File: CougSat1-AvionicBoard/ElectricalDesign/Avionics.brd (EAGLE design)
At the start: 160 x 100 mm, 213 parts, among them J1 +X Panel GPS, J10 iFJR SD1, J11 -Y, J12 +Z, J13 +X, J14 -Z, J15 +Y, J16 IFJR SD0, J2 IHU SD1, J3 SWD, J4 CougSat Card, J5 -X, J6 IHU SD0, J8 SWD, J9 SWD, U1 STM32L476RGT, U10 BNO055, U11 M24M01, U12 TXS0102DQM, U13 TXS0102DQM, U14 AD8515, U15 BNO055, U16 BNO055, U17 TXS0102DQM, U18 TXS0102DQM, U19 AD8515, U2 STM32L476RGT, U20 INA199C2, U21 INA199C2, U22 TXS0102DQM, U23 TXS0102DQM, U24 AD8515, U25 AD7291, U26 AD7291, U27 TXS0102DQM, U28 INA199C2, U29 AD8515, U3 STM32L476RGT, U30 DRV8837, U4 M24M01, U5 TXS0102DQM, U6 DRV8837, U7 DRV8837, U8 AD7291, U9 Venus838FLPx-L, Y1 8MHz ±10ppm, Y10 32.768kHz ±10ppm, Y2 32.768kHz ±10ppm, Y3 8MHz ±10ppm, Y4 32.768kHz ±10ppm, Y5 8MHz ±10ppm, Y6 32.768kHz ±10ppm, Y7 32.768kHz ±10ppm, Y8 32.768kHz ±10ppm

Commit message: Removed CTRL_RESET
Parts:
- moved R13 207.9 mm to (95.2, 218.5), turned to 90 degrees
- moved R4 205.7 mm to (112.9, 224.9)
- moved L1 191.6 mm to (112.9, 218.3)
- moved DS1 157.7 mm to (94.3, 221.2), turned to 180 degrees
- moved J4 117.0 mm to (0.00, 0.00)
- moved U2 9.32 mm to (66.8, 205.9)
- moved R43 3.50 mm to (79.0, 182.1)
- moved C4 0.20 mm to (90.7, 186.8)
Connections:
- removed net CTRL_!RESET: J4.A41, J4.B41, U1.37, U2.10, U3.38
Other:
- board size 160 x 100 mm -> 90.4 x 95.8 mm

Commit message: Placed Large Components
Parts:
- J4: device CougsInSpace-Boards:CARD-FULL-OPEN+X -> CougsInSpace-Boards:CARD-FULL
- moved J14 343.4 mm to (70.5, -38.0), turned to 90 degrees
- moved C16 329.8 mm to (64.9, -6.80), flipped to the bottom, turned to 270 degrees
- moved C12 324.4 mm to (86.1, 5.90), flipped to the bottom, turned to 270 degrees
- moved C60 322.9 mm to (56.0, -13.6), flipped to the bottom, turned to 180 degrees
- moved C61 321.3 mm to (49.5, -13.6), flipped to the bottom, turned to 180 degrees
- moved C63 318.4 mm to (56.5, 1.60), flipped to the bottom
- moved C62 312.2 mm to (45.4, -2.50), flipped to the bottom, turned to 270 degrees
- moved R36 311.6 mm to (45.5, 25.3), flipped to the bottom, turned to 270 degrees
- moved C9 310.5 mm to (64.9, -3.80), flipped to the bottom, turned to 270 degrees
- moved C21 310.2 mm to (52.4, 26.5), flipped to the bottom, turned to 180 degrees
- moved C11 310.0 mm to (76.9, 13.5), flipped to the bottom, turned to 180 degrees
- moved C20 305.4 mm to (49.5, 26.5), flipped to the bottom
- moved C10 304.3 mm to (72.9, 14.1), flipped to the bottom, turned to 90 degrees
- moved C83 303.5 mm to (46.1, -37.8), flipped to the bottom, turned to 90 degrees
- moved J11 303.2 mm to (47.5, -38.0), turned to 90 degrees
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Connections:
- new net IHU_GPIO-6: J4.A41, U3.37
- new net IHU_GPIO-7: J4.B41, U3.38
- net ADCS_BUS_SCL: now also U5.3; no longer U5.2
- net ADCS_BUS_SDA: now also U5.2; no longer U5.3
- net ADCS_JTCK: now also U12.3; no longer U12.2
- net ADCS_JTDI: now also U12.2; no longer U12.3
- net BUS_I2C0_SCL: now also U5.6; no longer U5.7
- net BUS_I2C0_SDA: now also U5.7; no longer U5.6
- net IFJR_BUS_MISO: now also U23.2; no longer U23.3
- net IFJR_BUS_SCK: now also U23.3; no longer U23.2
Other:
- outline, holes or cut-outs redrawn

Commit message: Finished Placing Components, Began Wiring
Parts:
- added C100, C101, C102, C43, C84, C99: 100nF 10%, CougsInSpace-Capacitors:1608
- moved C70 367.8 mm to (85.7, -14.1), flipped to the bottom, turned to 180 degrees
- moved C69 366.4 mm to (85.7, -15.8), flipped to the bottom, turned to 180 degrees
- moved C65 356.1 mm to (81.6, -19.9), flipped to the bottom, turned to 270 degrees
- moved C64 351.4 mm to (81.6, -17.0), flipped to the bottom, turned to 90 degrees
- moved C15 343.4 mm to (74.4, -19.9), flipped to the bottom, turned to 270 degrees
- moved R38 339.1 mm to (34.2, -14.7), flipped to the bottom, turned to 180 degrees
- moved C23 336.7 mm to (33.5, -19.8), flipped to the bottom, turned to 270 degrees
- moved R37 334.7 mm to (45.6, -2.60), flipped to the bottom, turned to 90 degrees
- moved C18 333.5 mm to (65.7, -4.20), flipped to the bottom, turned to 180 degrees
- moved R31 333.3 mm to (86.0, 19.9), flipped to the bottom
- moved C17 329.1 mm to (65.7, -1.80), flipped to the bottom, turned to 180 degrees
- moved C19 329.0 mm to (59.0, -0.80), flipped to the bottom, turned to 90 degrees
- moved U29 327.7 mm to (86.2, -19.0), flipped to the bottom, turned to 270 degrees
- moved U7 327.7 mm to (86.5, 15.5), flipped to the bottom, turned to 270 degrees
- moved R30 326.6 mm to (80.4, 19.9), flipped to the bottom
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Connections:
- removed net AVDD: C85.1, C86.1, C87.1
- net 3.3V_0: now also C101.1, C99.1
- net 3.3V_5: now also C100.1, C102.1
- net AGND: now also C43.2, C84.2
- net AVDD-0: now also C43.1, C85.1, C86.1, C87.1
- net AVDD-1: now also C84.1
- net DGND: now also C100.2, C101.2, C102.2, C99.2
- net IFJR_BUS_CS: now also U27.2; no longer U27.3
- net IFJR_BUS_MOSI: now also U27.3; no longer U27.2
- net IHU_JTCK: now also U17.3; no longer U17.2
- net IHU_JTDI: now also U17.2; no longer U17.3
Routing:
- net DGND: track 0.00 -> 61.0 mm
- net 3.3V_0: track 0.00 -> 11.6 mm
- net 3.3V_5: track 0.00 -> 8.23 mm
- net IHU_OSC_OUT: track 0.00 -> 4.56 mm
- net IFJR_OSC_OUT: track 0.00 -> 4.56 mm
- net 3.3V_2: track 0.00 -> 4.11 mm
- net IHU_SD_CS1: track 0.00 -> 3.55 mm
- net IFJR_OSC_32_IN: track 0.00 -> 2.07 mm
- net IFJR_OSC_32_OUT: track 0.00 -> 2.07 mm
- net IHU_OSC_32_IN: track 0.00 -> 2.07 mm
- net IHU_OSC_32_OUT: track 0.00 -> 2.07 mm
- net IHU_OSC_IN: track 0.00 -> 2.07 mm
- net IFJR_OSC_IN: track 0.00 -> 2.07 mm
- net IHU_SD_CS0: track 0.00 -> 2.02 mm
- net IHU_BOOT0: track 0.00 -> 1.93 mm
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
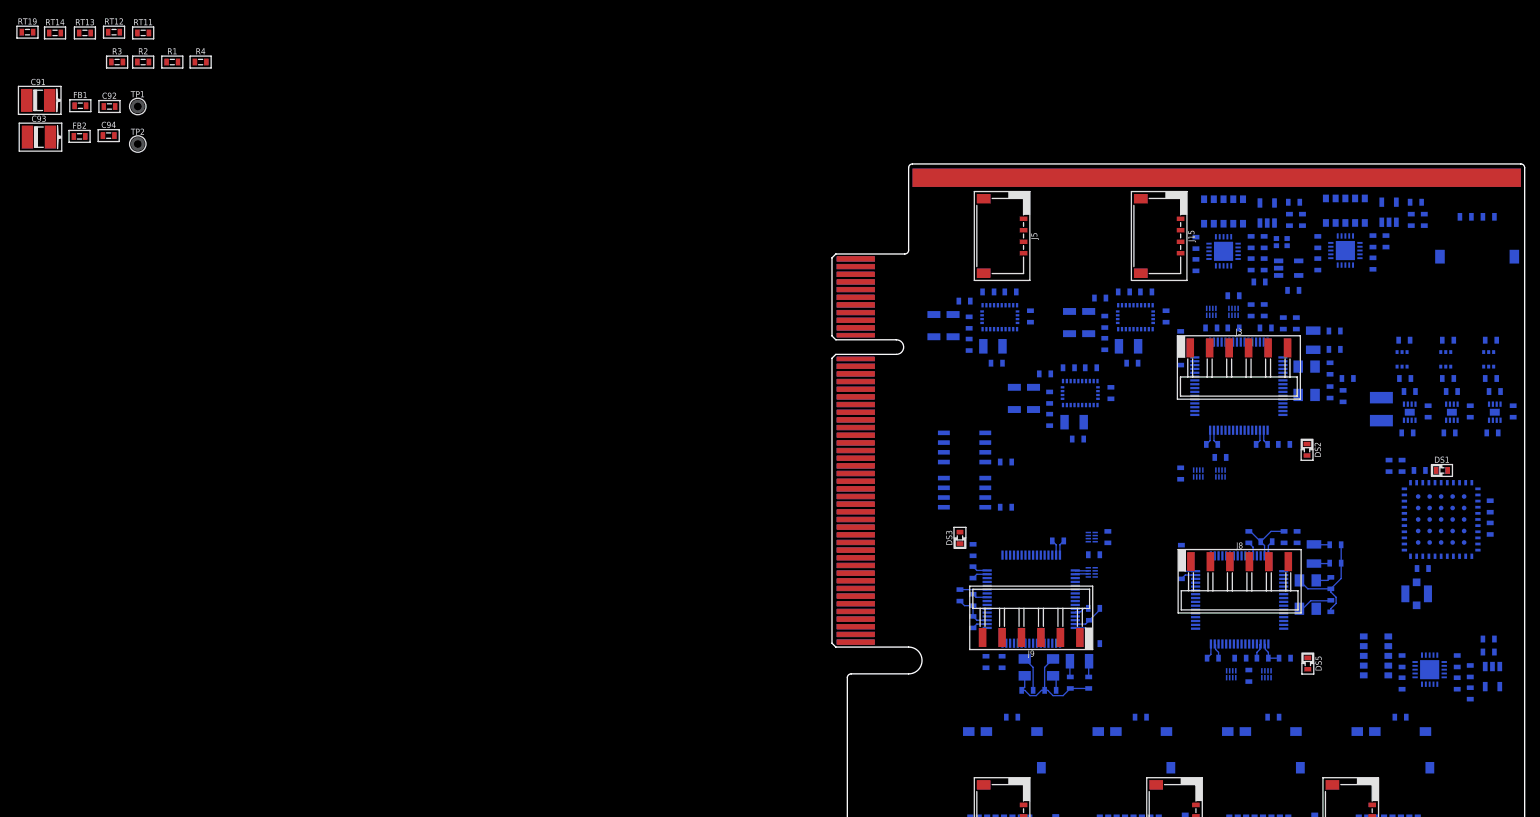
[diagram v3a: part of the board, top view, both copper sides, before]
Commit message: Placed AVDD Circuits and Ground Straps
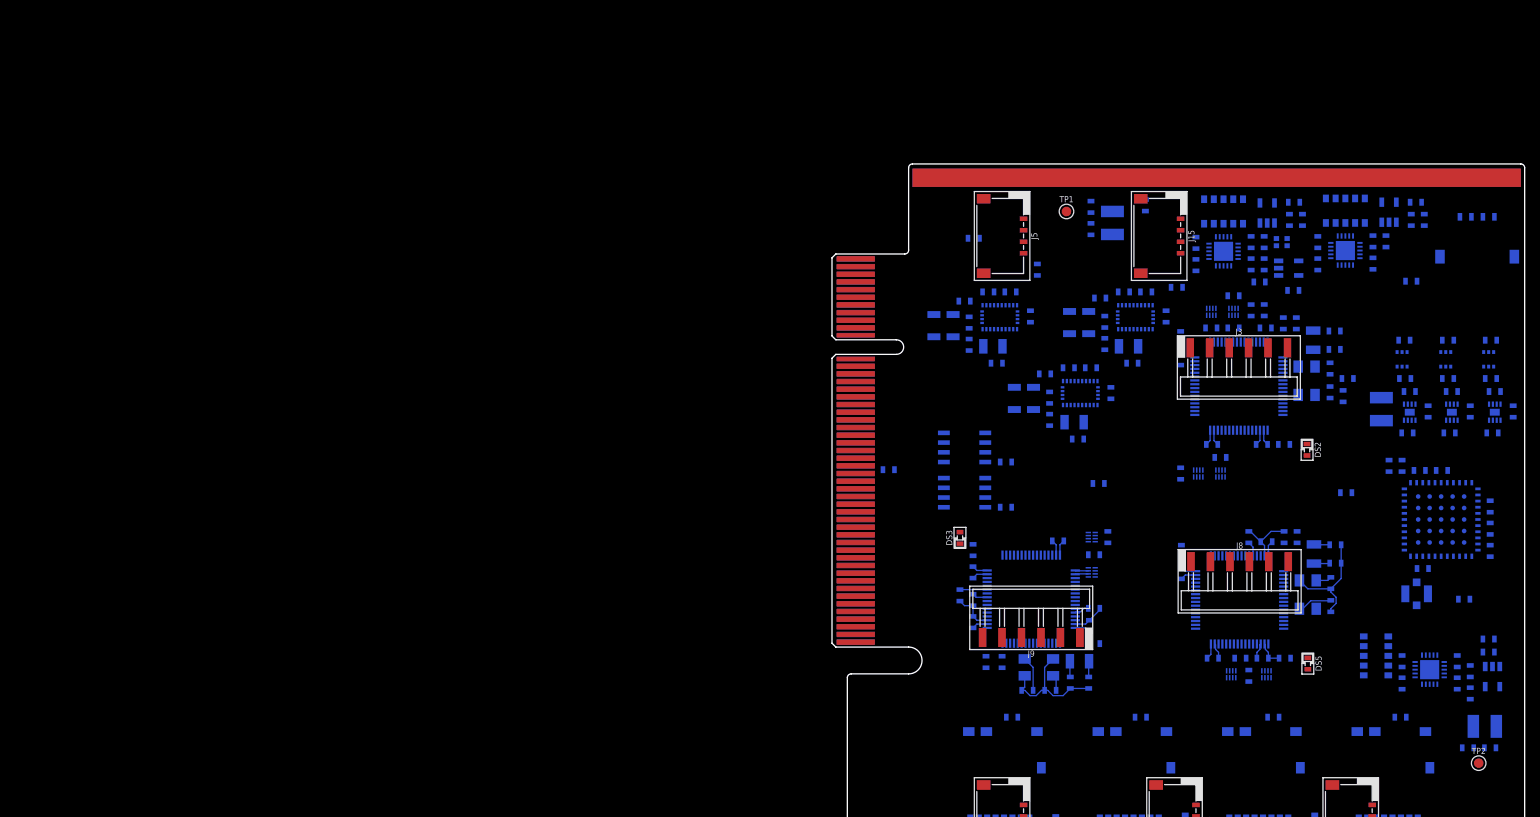
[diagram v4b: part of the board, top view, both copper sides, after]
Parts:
- TP1, TP2: value TEST_POINT-THT-1.0 -> TEST_POINT-SMD-C-1.25; device CougsInSpace-Connectors:THT-1.0 -> CougsInSpace-Connectors:SMD-C-1.25
- moved C93 203.8 mm to (85.2, -25.5), flipped to the bottom
- moved FB2 198.0 mm to (83.0, -28.3), flipped to the bottom, turned to 180 degrees
- moved C94 197.2 mm to (85.9, -28.3), flipped to the bottom, turned to 180 degrees
- moved RT13 194.6 mm to (82.5, -8.90), flipped to the bottom
- moved TP2 192.8 mm to (84.4, -30.3)
- moved RT19 182.3 mm to (67.1, 5.00), flipped to the bottom
- moved R4 180.0 mm to (85.9, -2.60), flipped to the bottom, turned to 90 degrees
- moved RT11 168.6 mm to (75.6, 32.6), flipped to the bottom
- moved RT14 148.4 mm to (34.8, 6.20), flipped to the bottom
- moved C91 141.1 mm to (36.6, 40.2), flipped to the bottom, turned to 90 degrees
- moved R2 138.1 mm to (45.0, 31.8), flipped to the bottom
- moved FB1 132.6 mm to (33.8, 42.3), flipped to the bottom, turned to 270 degrees
- moved C92 129.1 mm to (33.8, 39.4), flipped to the bottom, turned to 270 degrees
- moved R3 123.1 mm to (26.8, 34.1), flipped to the bottom, turned to 270 degrees
- moved TP1 122.0 mm to (30.6, 41.7)
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
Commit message: Routed Most Traces
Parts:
- removed C44, C51, C67: 1µF 10%, CougsInSpace-Capacitors:1608
- removed C50, C52, C68: 100nF 10%, CougsInSpace-Capacitors:1608
- moved C70 82.3 mm to (4.40, -26.9), turned to 90 degrees
- moved C69 80.4 mm to (6.10, -26.9), turned to 90 degrees
- moved U29 77.3 mm to (9.30, -26.4), turned to 180 degrees
- moved C64 75.6 mm to (7.30, -31.0), turned to 0 degrees
- moved C88 75.5 mm to (8.60, -29.3), turned to 180 degrees
- moved TP2 74.8 mm to (10.3, -20.2)
- moved C94 73.5 mm to (13.0, -19.3), turned to 0 degrees
- moved C65 72.3 mm to (10.2, -31.0), turned to 180 degrees
- moved C84 72.3 mm to (11.5, -29.3), turned to 180 degrees
- moved C93 71.6 mm to (13.7, -22.1), turned to 180 degrees
- moved U26 71.5 mm to (8.40, -34.6), turned to 180 degrees
- moved R7 70.4 mm to (7.30, -38.2), turned to 0 degrees
- moved RN3 69.2 mm to (6.60, -41.6), turned to 0 degrees
- moved FB2 67.7 mm to (15.9, -19.3), turned to 0 degrees
- moved C15 66.8 mm to (10.2, -38.2), turned to 180 degrees
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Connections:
- removed net COIL-X_OUT1: R29.1, U20.4, U30.2
- removed net COIL-Y_OUT1: R30.1, U21.4, U6.2
- removed net COIL-Z_OUT1: R31.1, U28.4, U7.2
- new net COIL-X_OUT2: R29.1, U20.4, U30.3
- new net COIL-Y_OUT2: R30.1, U21.4, U6.3
- new net COIL-Z_OUT2: R31.1, U28.4, U7.3
- net ADCS_ADC0_VREF: no longer RN1.3
- net ADCS_HALF_REF: no longer C44.1, C50.1
- net AGND: no longer C44.2, C50.2, C51.2, C52.2, C67.2, C68.2
- net AVREF-0: now also RN1.3; no longer C51.1, C52.1
- net AVREF-1: no longer C67.1, C68.1
- net COIL-X_!SLEEP: now also U2.27; no longer U2.20
- net COIL-X_COIL+: now also U30.2; no longer R29.2, U20.5
- net COIL-X_COIL-: now also R29.2, U20.5; no longer U30.3
- net COIL-X_IN1: now also U2.16; no longer U2.14
- net COIL-X_IN2: now also U2.17; no longer U2.15
- net COIL-Y_!SLEEP: now also U2.20; no longer U2.27
- net COIL-Y_COIL+: now also U6.2; no longer R30.2, U21.5
- net COIL-Y_COIL-: now also R30.2, U21.5; no longer U6.3
- net COIL-Y_IN1: now also U2.14; no longer U2.16
- net COIL-Y_IN2: now also U2.15; no longer U2.17
- net COIL-Z_COIL+: now also U7.2; no longer R31.2, U28.5
- net COIL-Z_COIL-: now also R31.2, U28.5; no longer U7.3
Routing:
- net DGND: track 61.0 -> 713.3 mm, vias 0 -> 85
- net 3.3V_2: track 4.11 -> 381.3 mm, vias 0 -> 43
- net AGND: track 0.00 -> 338.0 mm, vias 0 -> 33
- net ADCS_I2C1_SCL: track 0.00 -> 319.8 mm, vias 0 -> 2
- net ADCS_I2C1_SDA: track 0.00 -> 318.1 mm, vias 0 -> 3
- net PGND: track 0.00 -> 238.6 mm, vias 0 -> 9
- net COIL-Y_COIL+: track 0.00 -> 212.6 mm, vias 0 -> 3
- net COIL-Y_COIL-: track 0.00 -> 210.8 mm, vias 0 -> 3
- net CHASSIS: track 0.00 -> 204.6 mm, vias 0 -> 2
- net 3.3V_0: track 11.6 -> 189.5 mm, vias 0 -> 29
- net COIL-Z_COIL+: track 0.00 -> 177.2 mm, vias 0 -> 3
- net COIL-Z_COIL-: track 0.00 -> 173.1 mm, vias 0 -> 3
- net VBATT_5: track 0.00 -> 167.2 mm, vias 0 -> 4
- net 3.3V_5: track 8.23 -> 155.5 mm, vias 0 -> 20
- net BUS_JTAG_TMS: track 0.00 -> 132.1 mm, vias 0 -> 6
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
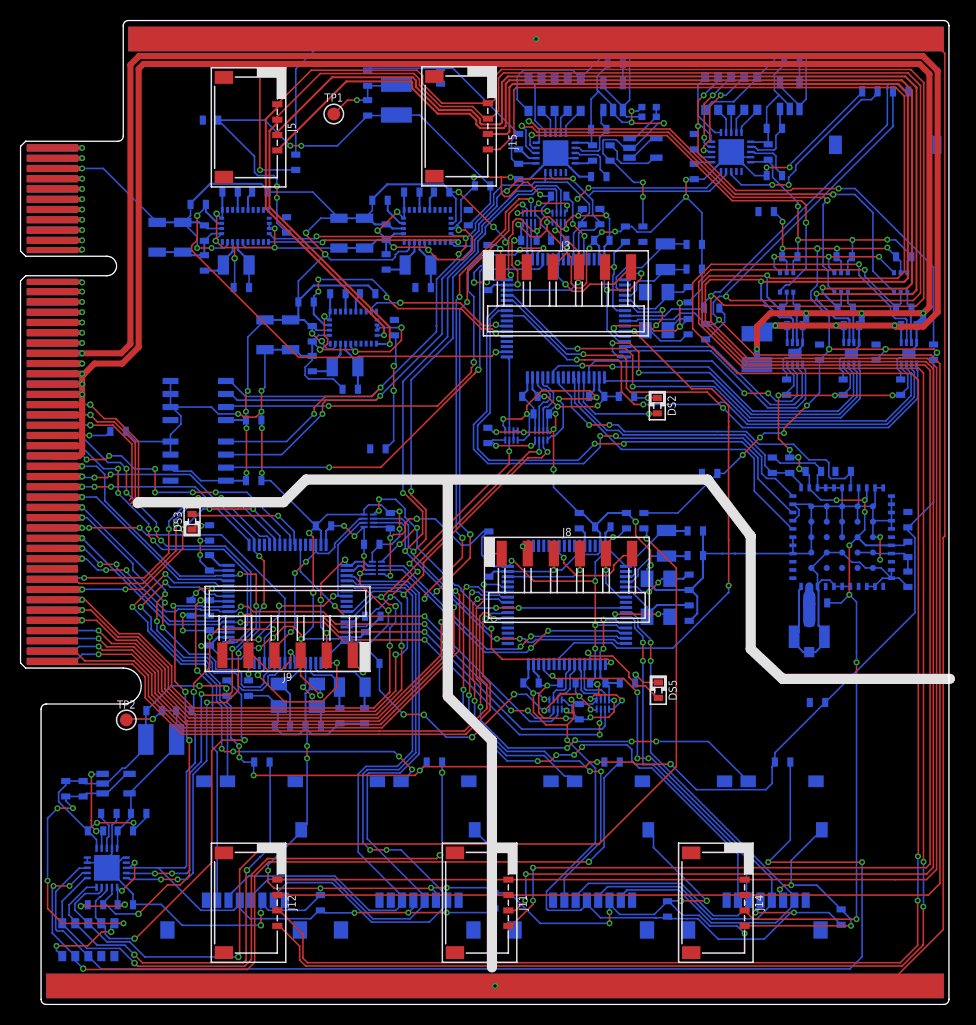
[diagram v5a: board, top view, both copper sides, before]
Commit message: Added Germination Payload Temperature ADC to C&DH-Design
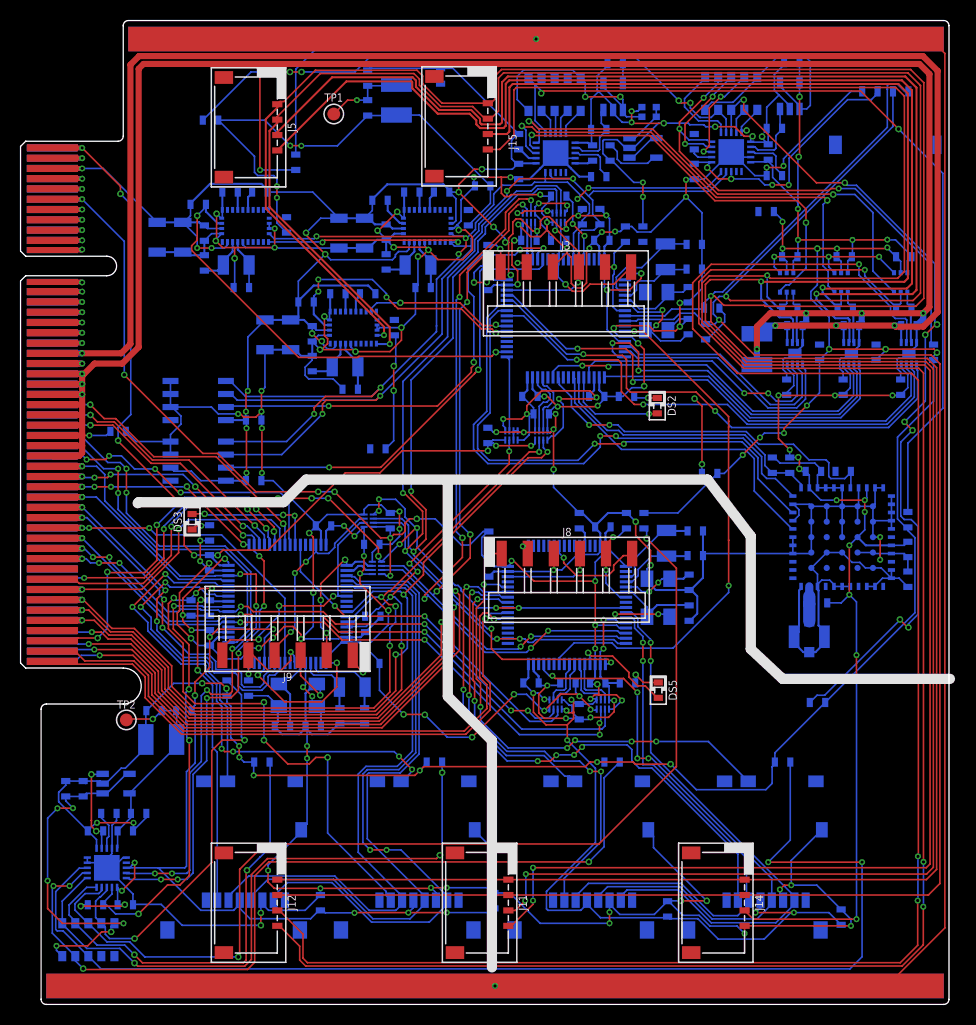
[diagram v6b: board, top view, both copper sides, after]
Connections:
- net IHU_GPIO-0: now also U3.40; no longer U3.14
- net IHU_GPIO-1: now also U3.36; no longer U3.15
- net IHU_GPIO-2: now also U3.35; no longer U3.16
- net IHU_GPIO-6: now also U3.38; no longer U3.37
- net IHU_GPIO-7: now also U3.37; no longer U3.38
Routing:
- net 3.3V_0: track 189.5 -> 275.9 mm, vias 29 -> 35
- net TEMP_PCB-2: track 2.20 -> 82.1 mm, vias 0 -> 8
- net TEMP_GPS: track 6.08 -> 84.1 mm, vias 0 -> 2
- net TEMP_PCB-1: track 2.52 -> 58.4 mm, vias 0 -> 4
- net 3.3V_5: track 155.5 -> 206.5 mm, vias 20 -> 23
- net IHU_SD_CS1: track 4.36 -> 52.0 mm, vias 2 -> 6
- net JTAG_EN_IHU: track 38.3 -> 83.1 mm, vias 6 -> 13
- net DGND: track 713.3 -> 740.7 mm, vias 85 -> 89
- net AVDD-0: track 50.8 -> 63.8 mm, vias 5 -> 7
- net IHU_GPIO-0: track 16.5 -> 29.4 mm, vias 1 -> 2
- net AGND: track 338.0 -> 350.6 mm, vias 33 -> 36
- net 3.3V_2: track 381.3 -> 393.7 mm, vias 43 -> 46
- net IHU_GPIO-2: track 14.1 -> 25.4 mm, vias 1 -> 2
- net IHU_GPIO-1: track 15.3 -> 26.4 mm, vias 1 -> 2
- net TEMP_PCB-4: track 2.84 -> 11.0 mm, vias 0 -> 3
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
